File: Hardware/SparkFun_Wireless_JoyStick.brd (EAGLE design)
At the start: 101.6 x 50.8 mm, 57 parts, among them J5 CORTEX_DEBUGPTH, Q2 2.5A/30V, U1 JOYSTICKPTH, U2 MCP73831, U3 AP2112K-3.3V, U4 JOYSTICKPTH, U6 ATSAMD21G-A, U7 74AHC1G125, Y2 32.768kHz

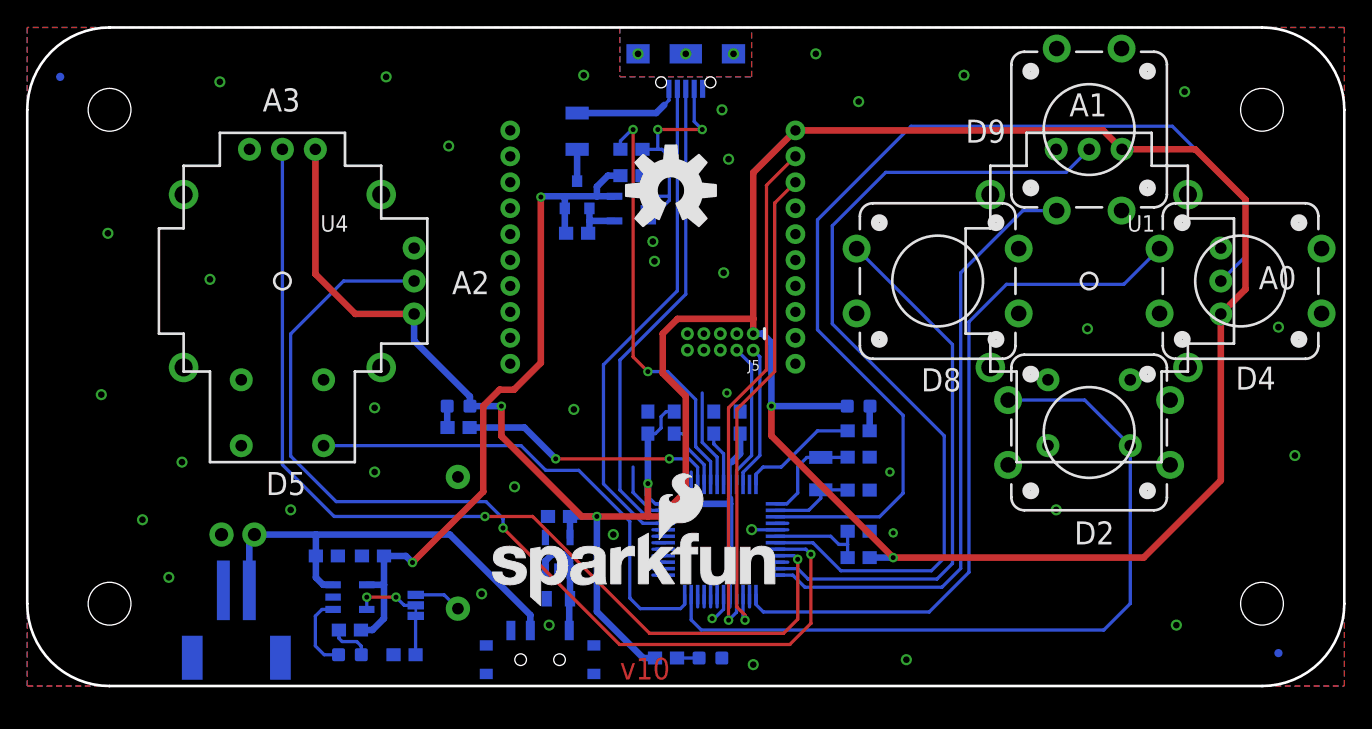
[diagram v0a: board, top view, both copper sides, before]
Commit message: V10 Updates
- Broke out extra pins
- Added LiPo fuel gauge
- Added "trigger" buttons
- Cleaned up layout
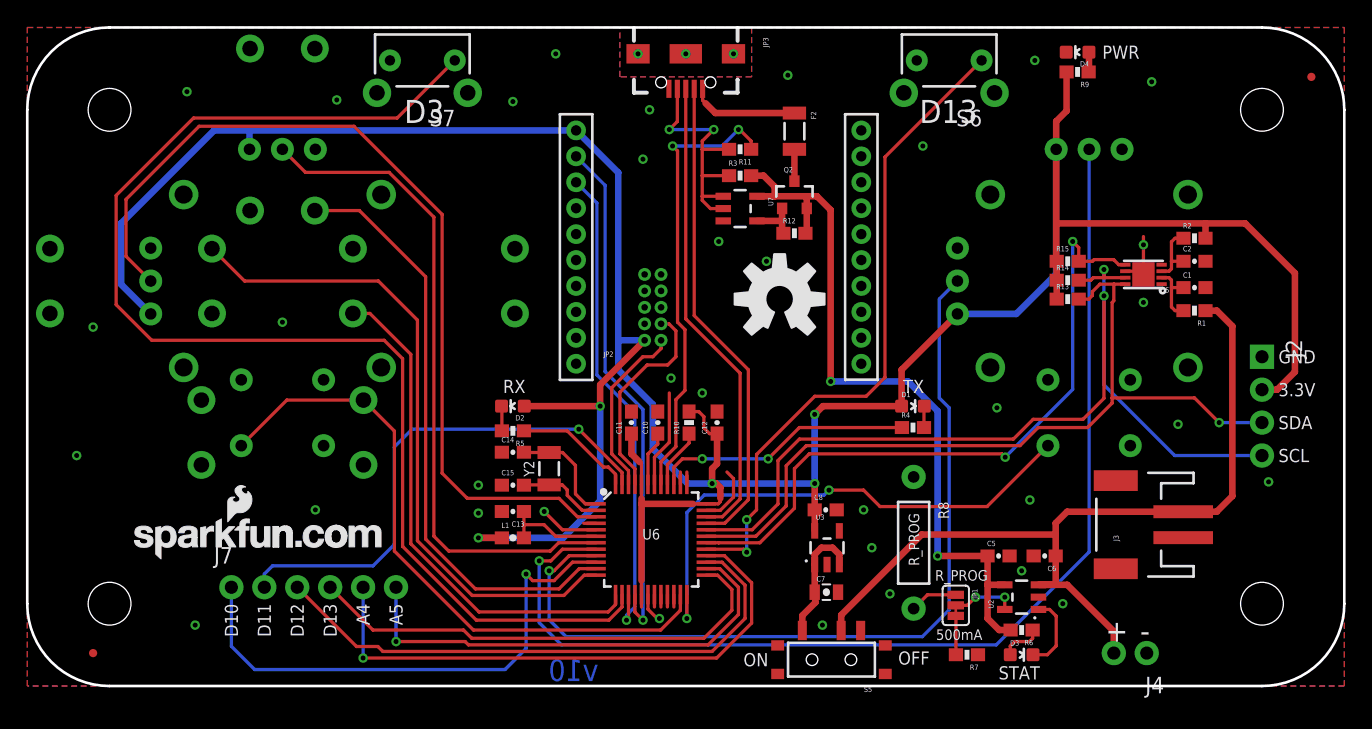
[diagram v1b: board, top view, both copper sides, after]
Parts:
- added C1: 1.0uF, SparkFun-Capacitors:0603-CAP
- added C2: 10nF, SparkFun-Capacitors:0603-CAP
- added J2: (no value), SparkFun-Connectors:1X04_NO_SILK
- added J7: (no value), SparkFun-Connectors:1X06_NO_SILK
- added R1: 1K, SparkFun-Resistors:0603-RES
- added R13, R14, R15: 4.7K, SparkFun-Resistors:0603-RES
- added R2: 180, SparkFun-Resistors:0603-RES
- added S6, S7: (no value), SparkFun-Electromechanical:TACTILE-PTH-SIDEEZ
- added U5: MAX1704X, SparkFun-PowerIC:TDFN-8
- LOGO2: value SFE_LOGO_NAME_FLAME.2_INCH -> SFE_LOGO_NAME_FLAME.3_INCH; device SparkFun-Aesthetics:SFE_LOGO_NAME_FLAME_.2 -> SparkFun-Aesthetics:SFE_LOGO_NAME_FLAME_.3
- R10, R6, R7, R9: device SparkFun-Resistors:0603-RES@1 -> SparkFun-Resistors:0603-RES
- moved FD2 96.5 mm to (99.1, 47.0), flipped to the top
- moved FD1 91.4 mm to (5.08, 2.54), flipped to the top
- moved H1 88.9 mm to (6.35, 6.35), flipped to the top
- moved H2 88.9 mm to (95.2, 6.35), flipped to the top
- moved H3 88.9 mm to (6.35, 44.5), flipped to the top
- moved H4 88.9 mm to (95.2, 44.5), flipped to the top
- moved S3 85.6 mm to (8.00, 31.2), flipped to the bottom
- moved U$1 75.7 mm to (8.26, 9.78), flipped to the top
- moved J4 72.0 mm to (86.4, 2.54), flipped to the top
- moved J3 69.9 mm to (85.5, 12.4), flipped to the top, turned to 90 degrees
- moved FRAME2 67.7 mm to (85.1, 34.3), flipped to the top, turned to 90 degrees
- moved S1 62.2 mm to (19.7, 42.9), flipped to the bottom
- moved S2 62.2 mm to (19.7, 19.6), flipped to the bottom
- moved U1 62.2 mm to (19.7, 31.2), flipped to the bottom
- moved U4 62.2 mm to (81.9, 31.2), flipped to the bottom
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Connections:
- removed net D10/SS: U6.27
- removed net D11/MOSI: U6.25
- removed net D12/MISO: U6.28
- removed net D13/SCK: U6.26
- removed net N$11: D1.C, R5.2
- removed net N$29: U6.47
- removed net N$32: U6.10
- new net A4: J7.1, U6.10
- new net A5: J7.2, U6.47
- new net D10: J7.3, U6.27
- new net D11: J7.4, U6.25
- new net D12: J7.5, U6.28
- new net D13: J7.6, U6.26
- new net N$1: D2.C, R5.2
- new net N$10: D1.C, R4.2
- new net N$16: C1.1, R1.2, U5.2
- net 3.3V: now also J2.2, R13.1, R14.1, R15.1, R2.2
- net A2: now also U4.H2; no longer U4.V2
- net A3: now also U4.V2; no longer U4.H2
- net D3: now also S7.1
- net D4: now also S4.1; no longer S3.1
- net D6: now also S6.1
- net D7: now also R15.2, U5.5
- net D8: now also S1.1; no longer S4.1
- net D9: now also S3.1; no longer S1.1
- net GND: now also C1.2, C2.2, J2.1, S6.2, S7.2, U5.1, U5.4, U5.6, U5.EP
- net N$12: now also C2.1, R2.1, U5.3; no longer D2.C, R4.2
- net SCL: now also J2.4, R14.2, U5.7
- net SDA: now also J2.3, R13.2, U5.8
- net VBAT: now also R1.1
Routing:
- net D3: track 0.96 -> 97.8 mm
- net SCL: track 0.96 -> 72.4 mm, vias 0 -> 2
- net SDA: track 0.96 -> 63.2 mm, vias 0 -> 1
- net D7: track 0.96 -> 52.1 mm, vias 0 -> 2
- net D6: track 0.96 -> 51.0 mm, vias 0 -> 2
- net D12: track 0.00 -> 44.0 mm, vias 0 -> 1
- net D10: track 0.00 -> 43.9 mm
- net A4: track 0.00 -> 40.6 mm, vias 0 -> 1
- net A5: track 0.00 -> 40.0 mm, vias 0 -> 1
- net D11: track 0.00 -> 37.6 mm
- net D13: track 0.00 -> 36.9 mm, vias 0 -> 1
- net VBAT: track 34.4 -> 65.5 mm
- net D4: track 55.1 -> 39.4 mm
- net A1: track 65.8 -> 51.7 mm
- net A2: track 76.1 -> 86.7 mm, vias 2 -> 1
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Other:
- board text added: "3.3V"
- board text added: "A4"
- board text added: "A5"
- board text added: "D10"
- board text added: "D11"
- board text added: "D12"
- board text added: "D13"
- board text added: "D3"
- board text added: "GND"
- board text added: "SCL"
- board text added: "SDA"
- board text added: "Wireless Joystick"

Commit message: V10 update
- Broke out a few more pins
- Cleaned up the schematic
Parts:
- removed U$1: SFE_LOGO_NAME_WEB, SparkFun-Aesthetics:SFE-NEW-WEBLOGO
- added J1: (no value), SparkFun-Connectors:1X06_NO_SILK
- added JP4: (no value), SparkFun-Passives:PAD-JUMPER-3-NC_BY_PASTE_YES_SILK_FULL_BOX
- D4: value RED -> BLUE
- JP1: device SparkFun-Passives:PAD-JUMPER-3-2OF3_NC_BY_TRACE_YES_SILK_FULL_BOX -> SparkFun-Passives:PAD-JUMPER-3-2OF3_NC_BY_PASTE_YES_SILK_FULL_BOX
- S5: value SWITCH_SPDT -> (none)
- moved FRAME2 80.5 mm to (21.6, -15.2), turned to 0 degrees
- moved LOGO3 54.0 mm to (58.0, 29.8)
- moved FRAME1 11.4 mm to (21.6, -15.2)
- moved J7 4.02 mm to (11.9, 6.35)
- moved J3 3.82 mm to (89.2, 13.5)
- moved R5 0.13 mm to (37.5, 19.8)
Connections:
- removed net N$13: R10.1, U6.40
- removed net N$7: U6.21
- new net SPI_MISO: J1.6, U6.21
- new net SPI_MOSI: J1.4, U6.19
- new net SPI_SCK: J1.5, U6.20
- net !RESET: now also R10.1, U6.40
- net 3.3V: now also J1.1, JP4.2; no longer R13.1, R14.1
- net GND: now also J1.2, J1.3
- net N$2: now also JP4.1, R14.1; no longer U6.19
- net N$3: now also JP4.3, R13.1; no longer U6.20
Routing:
- net SPI_MOSI: track 0.00 -> 34.5 mm
- net SPI_SCK: track 0.00 -> 32.4 mm
- net SPI_MISO: track 0.00 -> 29.8 mm
- net 3.3V: track 244.4 -> 270.7 mm
- net !RESET: track 0.00 -> 21.0 mm, vias 0 -> 1
- net D2: track 50.0 -> 56.2 mm, vias 0 -> 1
- net N$3: track 0.96 -> 5.66 mm
- net N$13: track 4.61 -> 0.00 mm
- net A5: track 40.0 -> 44.1 mm, vias 1 -> 2
- net GND: track 23.2 -> 26.0 mm, vias 35 -> 40
- net D10: track 43.9 -> 46.7 mm
- net D11: track 37.6 -> 40.3 mm
- net N$2: track 0.96 -> 3.44 mm
- net D9: track 51.3 -> 48.9 mm
- net VIN: track 57.7 -> 55.3 mm
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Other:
- board text added: "BAT"
- board text added: "D6"
- board text added: "I2C PU"
- board text added: "MISO"
- board text added: "MOSI"
- board text added: "SCK"

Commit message: V10 Updates
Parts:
- removed C13: 0.1uF, SparkFun-Capacitors:0603-CAP
- removed C15: 15pF, SparkFun-Capacitors:0603-CAP
- removed JP3: (no value), SparkFun-Connectors:USB-AB-MICRO-SMD_V03
- removed JP4: (no value), SparkFun-Passives:PAD-JUMPER-3-NC_BY_PASTE_YES_SILK_FULL_BOX
- added C3: 4.7uF, SparkFun-Capacitors:0603-CAP
- added C4: 1.0uF, SparkFun-Capacitors:0603-CAP
- added J6: (no value), SparkFun-Connectors:1X02_NO_SILK
- added TP1: TEST-POINT3, SparkFun-Passives:PAD.03X.03
- added U8: ATSAMD21G-A, SparkFun-DigitalIC:TQFP-48
- C1: device SparkFun-Capacitors:0603-CAP -> SparkFun-Capacitors:0805-CAP
- C10: value 0.1uF -> 15pF
- C2: value 10nF -> 2.2uF
- C5: value 4.7uF -> 10nF
- C7: value 1.0uF -> 0.1uF; device SparkFun-Capacitors:0805-CAP -> SparkFun-Capacitors:0603-CAP
- C8: value 2.2uF -> 0.1uF
- D1: value GREEN -> RED
- D2: value Yellow -> BLUE
- D3: value RED -> GREEN
- D4: value BLUE -> Yellow
- J1: device SparkFun-Connectors:1X06_NO_SILK -> SparkFun-Connectors:USB-AB-MICRO-SMD_V03
- J2: device SparkFun-Connectors:1X04_NO_SILK -> SparkFun-Connectors:1X06_NO_SILK
- J3: device SparkFun-Connectors:JST-2-SMD -> SparkFun-Connectors:1X06_NO_SILK
- J4: device SparkFun-Connectors:1X02_NO_SILK -> SparkFun-Connectors:1X04_NO_SILK
- J5: value CORTEX_DEBUGPTH -> (none); device SparkFun-Connectors:2X5-PTH-1.27MM -> SparkFun-Connectors:JST-2-SMD
- J7: value (none) -> CORTEX_DEBUGPTH; device SparkFun-Connectors:1X06_NO_SILK -> SparkFun-Connectors:2X5-PTH-1.27MM
- JP2: device SparkFun-RF:XBEE-1 -> SparkFun-Passives:PAD-JUMPER-3-NC_BY_PASTE_YES_SILK_FULL_BOX
- LOGO1: value OSHW-LOGOL -> SFE_LOGO_NAME_FLAME.3_INCH; device SparkFun-Aesthetics:OSHW-LOGO-L -> SparkFun-Aesthetics:SFE_LOGO_NAME_FLAME_.3
- LOGO2: value SFE_LOGO_NAME_FLAME.3_INCH -> OSHW-LOGOL; device SparkFun-Aesthetics:SFE_LOGO_NAME_FLAME_.3 -> SparkFun-Aesthetics:OSHW-LOGO-L
- R1: value 1K -> 100k
- R10: value 10K -> 4.7K
- R11: value 330 -> 4.7K
- R12: value 47K -> 4.7K
- R13: value 4.7K -> 10K
- R14, R15: value 4.7K -> 330
- R2: value 180 -> 330
- R3: value 100k -> 47K
- R4: value 330 -> 470
- R5: value 330 -> 1K
- R7: value 2.0k -> 180
- R8: value R_PROG -> 2.0k; device SparkFun-Resistors:AXIAL-0.4 -> SparkFun-Resistors:0603-RES
- R9: value 470 -> R_PROG; device SparkFun-Resistors:0603-RES -> SparkFun-Resistors:AXIAL-0.4
- S5: device SparkFun-Electromechanical:KPS-1290 -> SparkFun-Electromechanical:TACTILE-PTH-SIDEEZ
- S7: value (none) -> SWITCH_SPDT; device SparkFun-Electromechanical:TACTILE-PTH-SIDEEZ -> SparkFun-Electromechanical:KPS-1290
- U2: value MCP73831 -> JOYSTICKPTH; device SparkFun-PowerIC:SOT23-5 -> SparkFun-Electromechanical:JOYSTICK
- U3: value AP2112K-3.3V -> 74AHC1G125; device SparkFun-PowerIC:SOT23-5 -> SparkFun-DigitalIC:SOT23-5
- U4: value JOYSTICKPTH -> AP2112K-3.3V; device SparkFun-Electromechanical:JOYSTICK -> SparkFun-PowerIC:SOT23-5
- U5: value MAX1704X -> XBEE-2B3; device SparkFun-PowerIC:TDFN-8 -> SparkFun-RF:XBEE-SMD
- U6: value ATSAMD21G-A -> MAX1704X; device SparkFun-DigitalIC:TQFP-48 -> SparkFun-PowerIC:TDFN-8
- U7: value 74AHC1G125 -> MCP73831; device SparkFun-DigitalIC:SOT23-5 -> SparkFun-PowerIC:SOT23-5
- moved H3 96.7 mm to (95.2, 6.35)
- moved H4 96.7 mm to (6.35, 6.35)
- moved J2 84.9 mm to (11.9, 8.89), turned to 0 degrees
- moved J3 77.5 mm to (11.9, 6.35), turned to 0 degrees
- moved U1 62.2 mm to (81.9, 31.2)
- moved U2 62.0 mm to (19.7, 31.2), flipped to the bottom, turned to 180 degrees
- moved S7 56.0 mm to (62.0, 2.03), turned to 0 degrees
- moved J1 55.7 mm to (50.8, 48.8), turned to 270 degrees
- moved LOGO3 53.4 mm to (6.99, 14.2)
- moved R5 53.4 mm to (90.0, 29.0)
- moved D4 51.4 mm to (37.5, 21.6)
- moved S5 47.1 mm to (71.1, 48.3), turned to 180 degrees
- moved R15 44.7 mm to (37.5, 19.8), turned to 180 degrees
- moved J5 43.8 mm to (89.2, 13.5), flipped to the top
- moved D2 43.7 mm to (76.7, 2.41), turned to 270 degrees
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- renumbered C14 to C9, F2 to F1, Q2 to Q1, Y2 to Y1
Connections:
- net !RESET: now also J7.10, R13.1, U8.40; no longer J5.10, R10.1, U6.40
- net 3.3V: now also C2.1, D3.A, D4.A, J2.1, J4.2, J7.1, JP2.2, R12.1, R13.2, R4.2, R7.2, U2.H1, U2.V1, U4.5, U5.1, U8.17, U8.36, U8.44; no longer C11.1, D1.A, D2.A, J1.1, J2.2, J5.1, JP2.1, JP4.2, R10.2, R15.1, R2.2, R9.2, U3.5, U4.H1, U4.V1, U6.17, U6.36, U6.44
- net A0: now also U2.V2, U8.3; no longer U1.V2, U6.3
- net A1: now also U2.H2, U8.7; no longer U1.H2, U6.7
- net A2: now also U1.H2, U8.8; no longer U4.H2, U6.8
- net A3: now also U1.V2, U8.9; no longer U4.V2, U6.9
- net A4: now also J3.1, U8.10; no longer J7.1, U6.10
- net A5: now also J3.2, U8.47; no longer J7.2, U6.47
- net AREF: now also TP1.P$1, U8.4; no longer U6.4
- net D0/RXI: now also U5.2, U8.16; no longer JP2.2, U6.16
- net D1/TXO: now also U5.3, U8.15; no longer JP2.3, U6.15
- net D10: now also J3.3, U8.27; no longer J7.3, U6.27
- net D11: now also J3.4, U8.25; no longer J7.4, U6.25
- net D12: now also J3.5, U8.28; no longer J7.5, U6.28
- net D13: now also J3.6, U8.26; no longer J7.6, U6.26
- net D2: now also U2.B1A, U8.23; no longer U1.B1A, U6.23
- net D3: now also S6.1, U8.14; no longer S7.1, U6.14
- net D4: now also U8.13; no longer U6.13
- net D5: now also U1.B1A, U8.24; no longer U4.B1A, U6.24
- net D6: now also S5.1, U8.29; no longer S6.1, U6.29
- net D7: now also R12.2, U6.5, U8.30; no longer R15.2, U5.5, U6.30
- net D8: now also U8.11; no longer U6.11
- net D9: now also U8.12; no longer U6.12
- net GND: now also C10.1, C3.2, C4.2, D1.C, J1.GND1, J2.2, J2.3, J5.1, J6.1, J7.3, J7.5, R8.1, R9.P$1, S5.2, U2.B2A, U2.H3, U2.V3, U3.3, U4.2, U5.10, U6.1, U6.4, U6.6, U6.EP, U7.2, U8.18, U8.35, U8.42, U8.5; no longer C10.2, C13.2, C15.1, D4.C, J1.2, J1.3, J2.1, J3.1, J5.3, J5.5, JP2.10, JP3.GND1, R7.1, R8.P$1, S7.2, U2.2, U3.2, U4.B2A, U4.H3, U4.V3, U5.1, U5.4, U5.6, U5.EP, U6.18, U6.35, U6.42, U6.5, U7.3
- net N$1: now also D4.C, R15.2; no longer D2.C, R5.2
- net N$10: now also D3.C, R14.2; no longer D1.C, R4.2
- net N$12: now also C5.1, R7.1, U6.3; no longer C2.1, R2.1, U5.3
- net N$15: now also J1.ID1, R1.1, R2.2, U3.1, U3.2; no longer JP3.ID1, R11.2, R3.1, U7.1, U7.2
- net N$16: now also C4.1, R5.2, U6.2; no longer C1.1, R1.2, U5.2
- net N$17: now also R8.2; no longer R7.2
- net N$18: now also C11.1, U8.43; no longer C10.1, U6.43
- net N$19: now also D2.A; no longer D3.A
- net N$2: now also JP2.1, R11.1; no longer JP4.1, R14.1
- net N$20: now also D2.C, U7.1; no longer D3.C, U2.1
- net N$21: now also U8.1; no longer U6.1
- net N$22: now also C10.2, U8.2; no longer C15.2, U6.2
- net N$23: now also D1.A, R4.1; no longer D4.A, R9.1
- net N$24: now also C7.1, U8.6; no longer C13.1, U6.6
- net N$25: now also R3.1, U3.4; no longer R12.1, U7.4
- net N$3: now also JP2.3, R10.1; no longer JP4.3, R13.1
- net N$4: now also R9.P$2; no longer R8.P$2
- net N$5: now also U8.37; no longer U6.37
- net N$6: now also U8.38; no longer U6.38
- net N$8: now also U8.22; no longer U6.22
- net N$9: now also J1.VBUS1; no longer JP3.VBUS1
- net PROG: now also U7.5; no longer U2.5
- net RX_LED: now also R15.1, U8.48; no longer R5.1, U6.48
- net SCL: now also J4.4, R11.2, U6.7, U8.32; no longer J2.4, R14.2, U5.7, U6.32
- net SDA: now also J4.3, R10.2, U6.8, U8.31; no longer J2.3, R13.2, U5.8, U6.31
- net SHIELD: now also J1.SHIELD1, J1.SHIELD2, J1.SHIELD3; no longer JP3.SHIELD1, JP3.SHIELD2, JP3.SHIELD3
- net SPI_MISO: now also J2.6, U8.21; no longer J1.6, U6.21
- net SPI_MOSI: now also J2.4, U8.19; no longer J1.4, U6.19
- net SPI_SCK: now also J2.5, U8.20; no longer J1.5, U6.20
- net SWCLK: now also J7.4, U8.45; no longer J5.4, U6.45
- net SWDIO: now also J7.2, U8.46; no longer J5.2, U6.46
- net TX_LED: now also R14.1, U8.39; no longer R4.1, U6.39
- net USB_D+: now also J1.D+1, U8.34; no longer JP3.D+1, U6.34
- net USB_D-: now also J1.D-1, U8.33; no longer JP3.D-1, U6.33
- net USB_HOST_EN: now also R2.1, U8.41; no longer R11.1, U6.41
- net VBAT: now also J5.2, J6.2, R5.1, S7.P, U7.3; no longer J3.2, J4.2, R1.1, S5.P, U2.3
- net VBAT_SW: now also C1.1, S7.O, U4.1, U4.3; no longer C7.1, S5.O, U3.1, U3.3
- net VIN: now also C3.1, R1.2, U3.5, U7.4; no longer C5.1, R12.2, U2.4, U7.5
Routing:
- net 3.3V: track 270.7 -> 277.4 mm, vias 5 -> 6
- net AREF: track 0.96 -> 3.49 mm
- net D0/RXI: track 39.6 -> 42.1 mm, vias 1 -> 2
- net A5: track 44.1 -> 46.6 mm
- net D1/TXO: track 37.4 -> 39.2 mm, vias 1 -> 2
- net VIN: track 55.3 -> 54.2 mm
- net D6: track 51.0 -> 52.0 mm
- net GND: track 26.0 -> 25.3 mm
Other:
- board text added: "AREF"

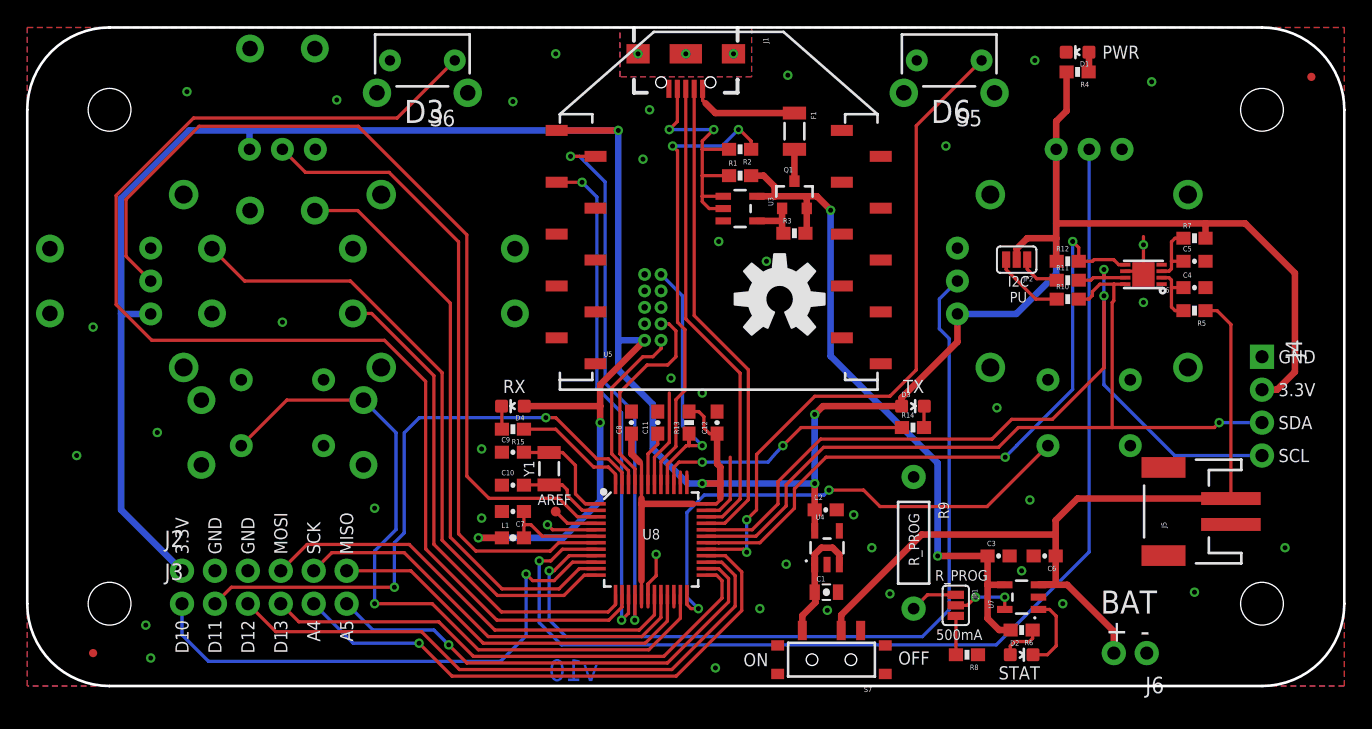
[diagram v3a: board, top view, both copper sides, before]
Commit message: Design Review Changes
- Added LED to D13 for low batt indication.
- Added test points for bootloader programming from testbed
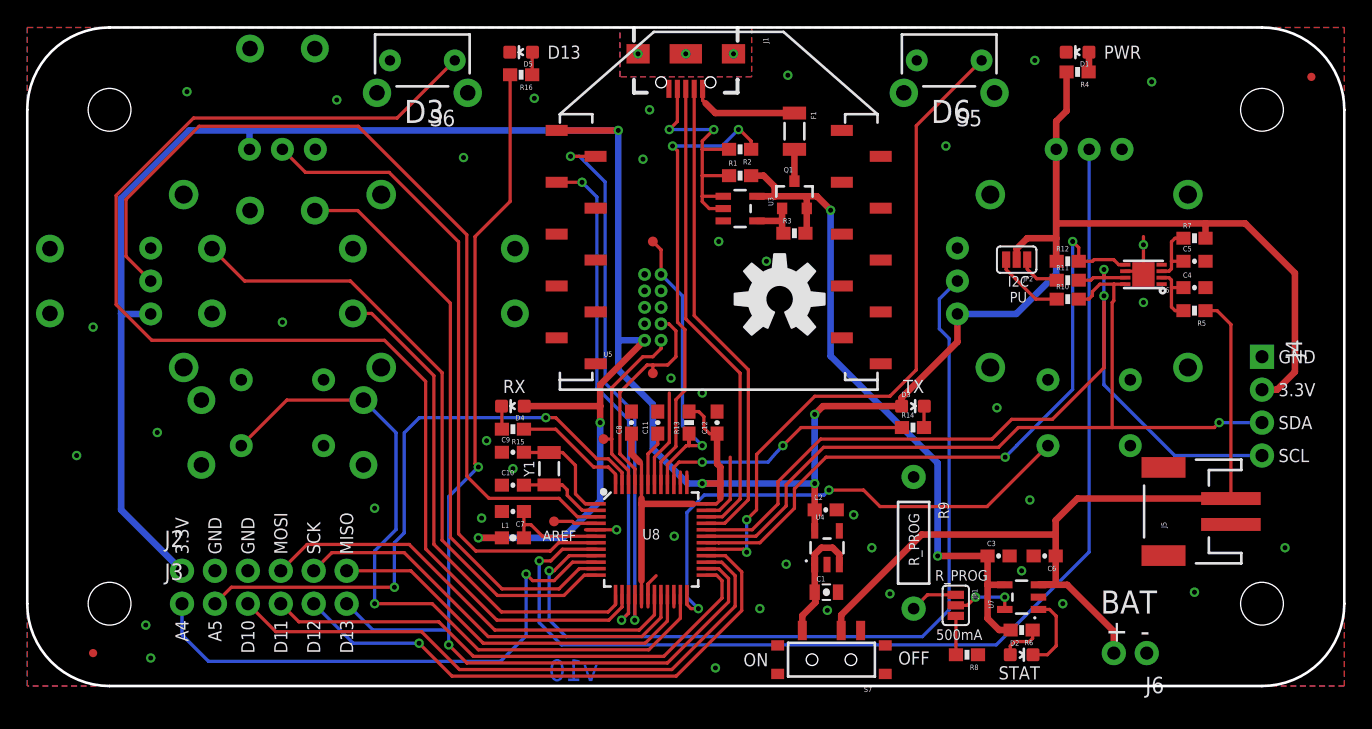
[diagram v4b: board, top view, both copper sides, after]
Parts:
- added D5: RED, SparkFun-LED:LED-0603
- added R16: 470, SparkFun-Resistors:0603-RES
- added TP2, TP3, TP4: (no value), SparkFun-Passives:PAD.03X.03
- TP1: value TEST-POINT3 -> (none)
- moved TP1 0.77 mm to (40.6, 12.7)
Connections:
- new net N$7: D5.A, R16.1
- net !RESET: now also TP4.P$1
- net D13: now also R16.2
- net GND: now also D5.C
- net SWCLK: now also TP3.P$1
- net SWDIO: now also TP2.P$1
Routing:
- net D13: track 37.1 -> 82.8 mm, vias 1 -> 2
- net GND: track 25.3 -> 22.1 mm, vias 40 -> 41
- net !RESET: track 21.0 -> 23.8 mm
- net N$7: track 0.00 -> 1.77 mm
- net SWDIO: track 13.7 -> 14.3 mm
- net SWCLK: track 16.4 -> 17.0 mm
